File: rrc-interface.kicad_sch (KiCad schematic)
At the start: 47 parts, among them J1 Mic Jack, J10 Input Only Pins, J11 Input Only Pins, J12 Flash mode, J15 RRC Optional Config DIP Socket, J2 To RRC, J3 6P6C RRC, J4 Audio Out, J5 Ptt, J6 TF Set, J8 UART Socket, J9 SPI Breakout, U1 ESP32-DevKitC, U2 ADP1108AN, U3 ADG884xRM

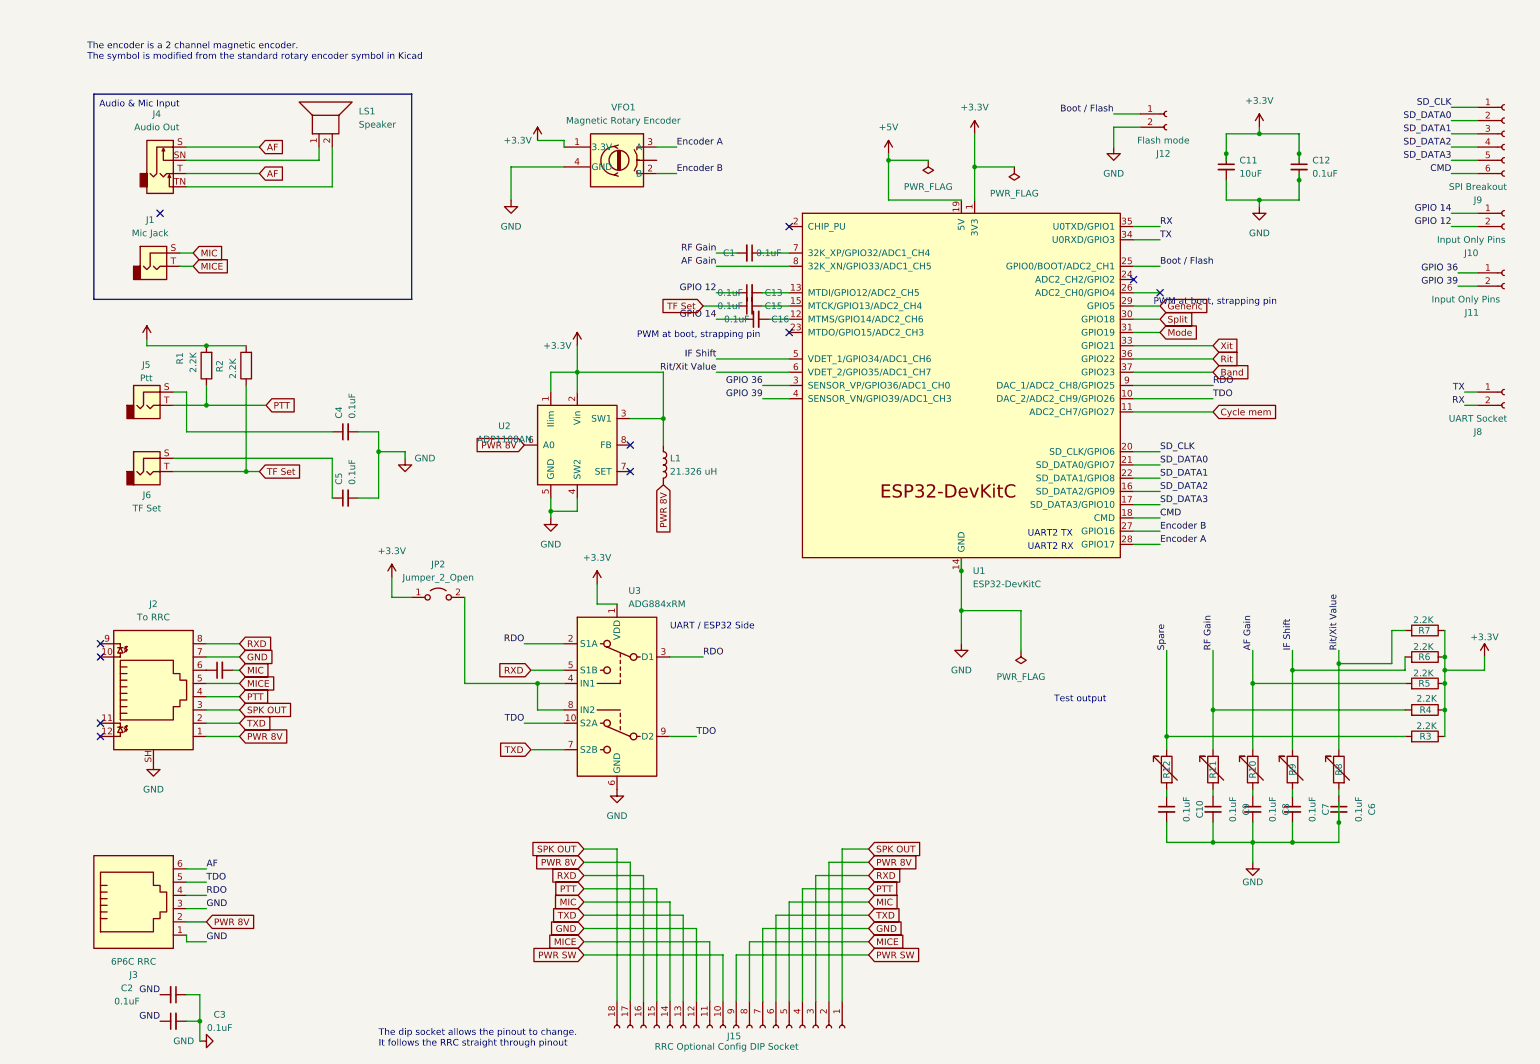
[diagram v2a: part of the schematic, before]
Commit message: update main board routing, add 3d models and improve layout
Changes:

* update main board layout a bit
* try to improve routing
* add 3d model for 6p6c
* add decoupling caps to ptt line
* almost finish pot board
* switch board almost finished

Details:
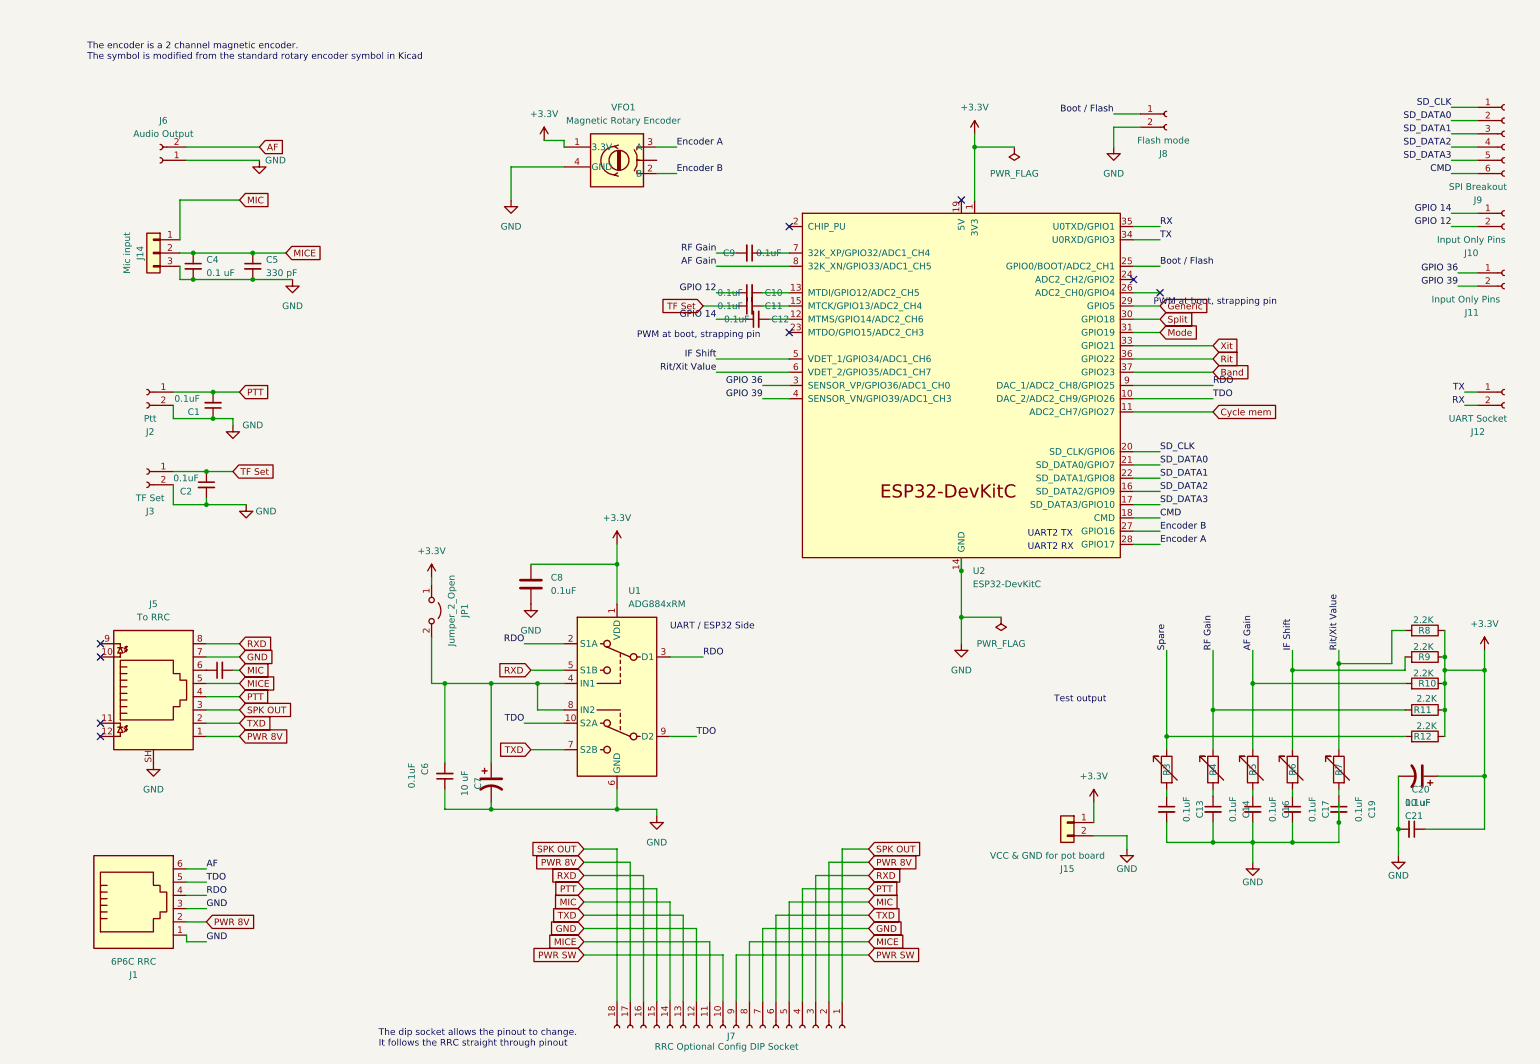
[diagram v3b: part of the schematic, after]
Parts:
- removed C11: 10uF, Capacitor_SMD:C_0603_1608Metric, symbol Device:C_Small
- removed C12, C3: 0.1uF, Capacitor_SMD:C_0603_1608Metric, symbol Device:C_Small
- removed J1: Mic Jack, Connector_Audio:Jack_3.5mm_CUI_SJ1-3523N_Horizontal, symbol Connector_Audio:AudioJack2
- removed J4: Audio Out, Connector_Audio:Jack_3.5mm_CUI_SJ1-3535NG_Horizontal, symbol Connector_Audio:AudioJack2_Switch
- removed J5: Ptt, Connector_Audio:Jack_3.5mm_CUI_SJ1-3523N_Horizontal, symbol Connector_Audio:AudioJack2
- removed J6: TF Set, Connector_Audio:Jack_3.5mm_CUI_SJ1-3523N_Horizontal, symbol Connector_Audio:AudioJack2
- removed L1: 21.326 uH, symbol Device:L
- removed LS1: Speaker, Connector_PinHeader_2.54mm:PinHeader_1x02_P2.54mm_Vertical, symbol Device:Speaker
- removed R1, R2: 2.2K, Resistor_SMD:R_0603_1608Metric, symbol Device:R
- removed U2: ADP1108AN, Package_DIP:DIP-8_W7.62mm, symbol Regulator_Switching:ADP1108AN
- added C1, C21, C6: 0.1uF, Capacitor_SMD:C_0603_1608Metric, symbol Device:C_Small
- added C20, C7: 10 uF, Capacitor_SMD:CP_Elec_3x5.3, symbol Device:C_Polarized_US
- added C8: 0.1uF, Capacitor_SMD:C_0402_1005Metric, symbol Device:C
- added J14: Mic input, Connector_JST:JST_PH_B3B-PH-K_1x03_P2.00mm_Vertical, symbol Connector_Generic:Conn_01x03
- added J15: VCC & GND for pot board, Connector_JST:JST_PH_B2B-PH-K_1x02_P2.00mm_Vertical, symbol Connector_Generic:Conn_01x02
- added J2: Ptt, Connector_JST:JST_PH_B2B-PH-K_1x02_P2.00mm_Vertical, symbol Connector:Conn_01x02_Socket
- added J3: TF Set, Connector_JST:JST_PH_B2B-PH-K_1x02_P2.00mm_Vertical, symbol Connector:Conn_01x02_Socket
- added J6: Audio Output, Connector_JST:JST_PH_B2B-PH-K_1x02_P2.00mm_Vertical, symbol Connector:Conn_01x02_Socket
- C4: value 0.1uF -> 0.1 uF
- C5: value 0.1uF -> 330 pF
- J1: renamed from J3; footprint Connector_RJ:RJ12_Amphenol_54601 -> Library:RJ12_Amphenol_54601
- JP1: renamed from JP2; footprint (none) -> Connector_PinHeader_2.54mm:PinHeader_1x02_P2.54mm_Vertical
- renumbered C13 to C10, C15 to C11, C16 to C12, C10 to C13, C9 to C14, C8 to C16, C7 to C17, C6 to C19, C14 to C3, C1 to C9, J8 to J12, J2 to J5, J15 to J7, J12 to J8, R5 to R10, R4 to R11, R3 to R12, R12 to R3, R11 to R4, R10 to R5, R9 to R6, R8 to R7, R7 to R8, R6 to R9, U3 to U1, U1 to U2
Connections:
- net AF: now also J6.2 (Pin_2)
- net GND: now also C1.1, C20.2, C21.2, C6.1, C7.2, C8.1, J14.3 (Pin_3), J15.2 (Pin_2), J2.2 (Pin_2), J3.2 (Pin_2), J6.1 (Pin_1); no longer C2.1
- net MIC: now also J14.1 (Pin_1)
- net MICE: now also C4.1, C5.1, J14.2 (Pin_2)
- net PTT: now also C1.2, J2.1 (Pin_1)
- net TF Set: now also C2.1, J3.1 (Pin_1)
- net at JP1.2 (B), U1.4 (IN1), U1.8 (IN2): now also C6.2, C7.1
- net +3V3 renamed +3.3V
- net +3.3V: now also C20.1, C21.1, C8.2, J15.1 (Pin_1)
- net +5V: no longer names the net of U2.19 (5V)
- no-connect marks 11 -> 9
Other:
- moved on the sheet: JP1
